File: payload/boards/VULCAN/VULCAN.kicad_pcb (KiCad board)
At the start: 2 copper layers, 63.5 x 101.6 mm, 74 parts, among them IC1 LT1001CS8#PBF, J1 POWER, J2 I2C, J3 Serial, J4 SPI, J5 GPIO, J6 XT60PW-M, J7 Screw_Terminal_01x06, J8 Screw_Terminal_01x06, J9 FAN, Q1 2N7002K, U1 DS18B20, U2 AZ1117IH-5.0TRG1, U3 AP63357, U4 MPXV7002DP, U5 DEV-16771, U6 MAX31850KATB+T, U7 MAX31850KATB+T, U8 MAX31850KATB+T

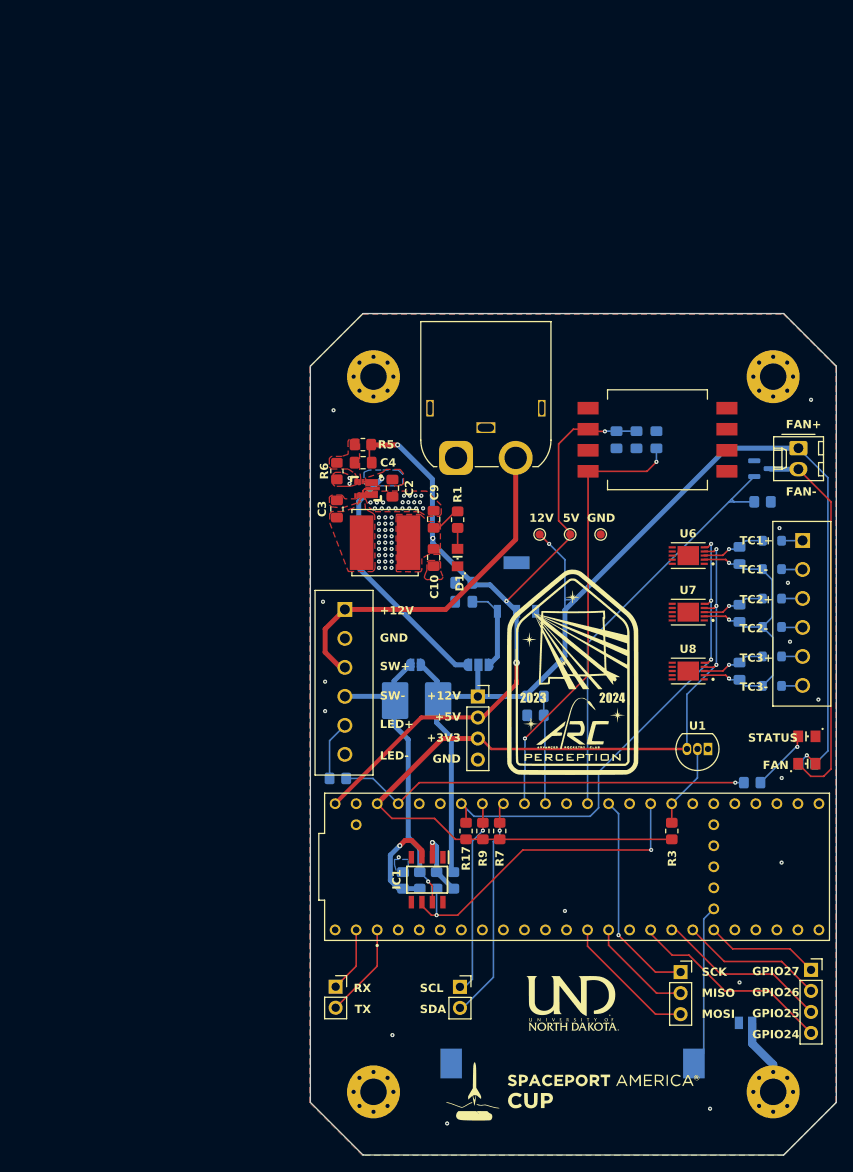
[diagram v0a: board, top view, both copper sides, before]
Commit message: rework
boost converter stuff
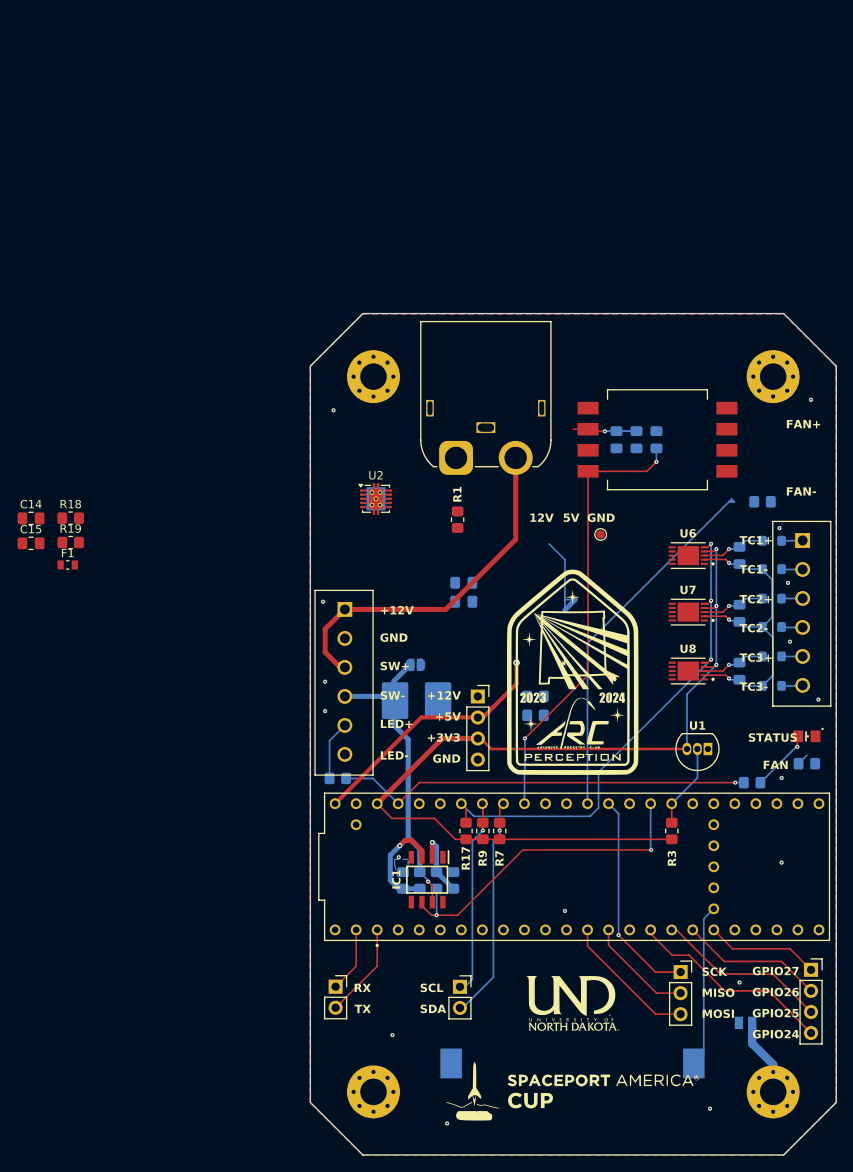
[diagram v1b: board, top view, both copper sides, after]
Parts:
- removed C10, C9: 22uF, Capacitor_SMD:C_0805_2012Metric_Pad1.18x1.45mm_HandSolder
- removed C2: 10uF, Capacitor_SMD:C_0805_2012Metric_Pad1.18x1.45mm_HandSolder
- removed C3: 0.1u, Capacitor_SMD:C_0805_2012Metric_Pad1.18x1.45mm_HandSolder
- removed C4: 47pF, Capacitor_SMD:C_0805_2012Metric_Pad1.18x1.45mm_HandSolder
- removed D1: OSRAM_LSR976-NR-1, Skyhawkson_Footprints:OSRAM_0805
- removed D3: CMD17-21VGD/TR8, Skyhawkson_Footprints:OSRAM_0805
- removed J9: FAN, CustomFootprintLib:Molex_KK-254_AE-6410-02A_1x02_P2.54mm_Vertical
- removed JP1: Jumper_3_Open, Jumper:SolderJumper-3_P1.3mm_Open_RoundedPad1.0x1.5mm
- removed L1: 6.8uH, CustomFootprintLib:IND_SRN8040TA-6R8M
- removed Q1: 2N7002K, Package_TO_SOT_SMD:SOT-23
- removed R5: 220k, Resistor_SMD:R_0805_2012Metric_Pad1.20x1.40mm_HandSolder
- removed R6: 41.2k, Resistor_SMD:R_0805_2012Metric_Pad1.20x1.40mm_HandSolder
- removed TP2: VIN, TestPoint:TestPoint_Pad_D1.0mm
- removed TP3: +5V, TestPoint:TestPoint_Pad_D1.0mm
- removed U3: AP63357, CustomFootprintLib:AP63356 (V-DFN3020-13)
- added C14: 10uF, Capacitor_SMD:C_0805_2012Metric_Pad1.18x1.45mm_HandSolder, F.Cu at (118.7, 70.5)
- added C15: 10uF, Capacitor_SMD:C_0805_2012Metric_Pad1.18x1.45mm_HandSolder, F.Cu at (118.7, 73.5)
- added F1: LF_0494003, Skyhawkson_Footprints:LF_0494_(0603), F.Cu at (123.1, 76.1)
- added R18: 2M, Resistor_SMD:R_0805_2012Metric_Pad1.20x1.40mm_HandSolder, F.Cu at (123.5, 70.4)
- added R19: 220k, Resistor_SMD:R_0805_2012Metric_Pad1.20x1.40mm_HandSolder, F.Cu at (123.5, 73.4)
- C1: value 22uF -> 10uF
- C5: value 10uF -> 1uF
- R10: value 500 -> 2M
- R8: value 470 -> 220k
- U2: value AZ1117IH-5.0TRG1 -> TPS61200DRC; footprint CustomFootprintLib:SOT223-5_DIO -> Package_SON:Texas_S-PVSON-N10_ThermalVias; moved to F.Cu
- moved U2 20.0 mm to (160.3, 68.1), turned to 0 degrees
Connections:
- net /+12V_RAW renamed /VBAT_SWITCH
- net /+BATT_RAW renamed /VBAT
- net /DS18_TEMP renamed /BOARD_TEMP
- C1 pad 1: +5V -> GND
- C1 pad 2: GND -> /VCC
- C12 pad 1: +5V -> /+5V
- C13 pad 1: +5V -> /+5V
- C5 pad 1: 5V_LDO -> Net-(U2-VAUX)
- J1 pad 2: +5V -> /+5V
- JP3 pad 1: /+12V -> /VCC
- R1 pad 1: +5V -> /+5V
- R10 pad 1: /+12V -> /+5V
- R10 pad 2: Net-(D3-PadA) -> Net-(U2-FB)
- R11 pad 1: /+12V -> /VCC
- R11 pad 2: /VBAT_SENSE -> /VCC_SENSE
- R12 pad 1: /VBAT_SENSE -> /VCC_SENSE
- R14 pad 1: /+12V -> /VCC
- R8 pad 1: GND -> Net-(U2-FB)
- R8 pad 2: /FAN -> GND
- R_Shunt1 pad 1: /+12V -> /VCC
- U2 pad 1: GND -> Net-(U2-VAUX)
- U2 pad 2: +5V -> /+5V
- U2 pad 3: 5V_LDO -> Net-(U2-L)
- U2 pad 4: unconnected-(U2-VOUT-Pad4) -> GND
- U4 pad 2: +5V -> /+5V
- U5 pad VIN: +5V -> /+5V
- U6 pad 6: unconnected-(U6-AD0-Pad6) -> GND
- U6 pad 7: unconnected-(U6-AD1-Pad7) -> GND
- U6 pad 8: unconnected-(U6-AD2-Pad8) -> GND
- U6 pad 9: unconnected-(U6-AD3-Pad9) -> GND
- U7 pad 6: unconnected-(U7-AD0-Pad6) -> +3V3
- U7 pad 7: unconnected-(U7-AD1-Pad7) -> GND
- U7 pad 8: unconnected-(U7-AD2-Pad8) -> GND
- U7 pad 9: unconnected-(U7-AD3-Pad9) -> GND
- U8 pad 6: unconnected-(U8-AD0-Pad6) -> GND
- U8 pad 7: unconnected-(U8-AD1-Pad7) -> +3V3
- U8 pad 8: unconnected-(U8-AD2-Pad8) -> GND
- U8 pad 9: unconnected-(U8-AD3-Pad9) -> GND
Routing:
- net /+12V: track 142.5 -> 11.8 mm, vias 1 -> 0
- net +5V: track 105.8 -> 0.00 mm, vias 5 -> 0
- net Net-(J9-Pin_2): track 46.2 -> 0.00 mm
- net /+5V: track 0.00 -> 37.8 mm, vias 0 -> 2
- net 5V_BUCK: track 30.9 -> 0.00 mm, vias 1 -> 0
- net /VBAT_SENSE: track 13.0 -> 0.00 mm
- net 5V_LDO: track 10.4 -> 0.00 mm
- net /FAN: track 51.3 -> 45.1 mm
- net Net-(D3-PadA): track 2.90 -> 0.00 mm, vias 1 -> 0
- net Net-(D1-PadA): track 2.51 -> 0.00 mm
- net Net-(U3-SW): track 1.87 -> 0.00 mm
- net Net-(U2-FB): track 0.00 -> 1.41 mm
- net /I2C_SCL: track 24.1 -> 23.0 mm
- net /I2C_SDA: track 27.5 -> 26.7 mm
- net GND: track 0.28 -> 0.00 mm, vias 65 -> 17
- removed copper zone on F.Cu, net +5V
- removed copper zone on B.Cu, net 5V_BUCK
- removed copper zone on F.Cu, net 5V_BUCK
- removed copper zone on F.Cu, net Net-(U3-BST)
- removed copper zone on F.Cu, net Net-(U3-FB)
- removed copper zone on F.Cu, net Net-(U3-SW)

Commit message: reverted back to bucks
since we need weight in the form of batteries
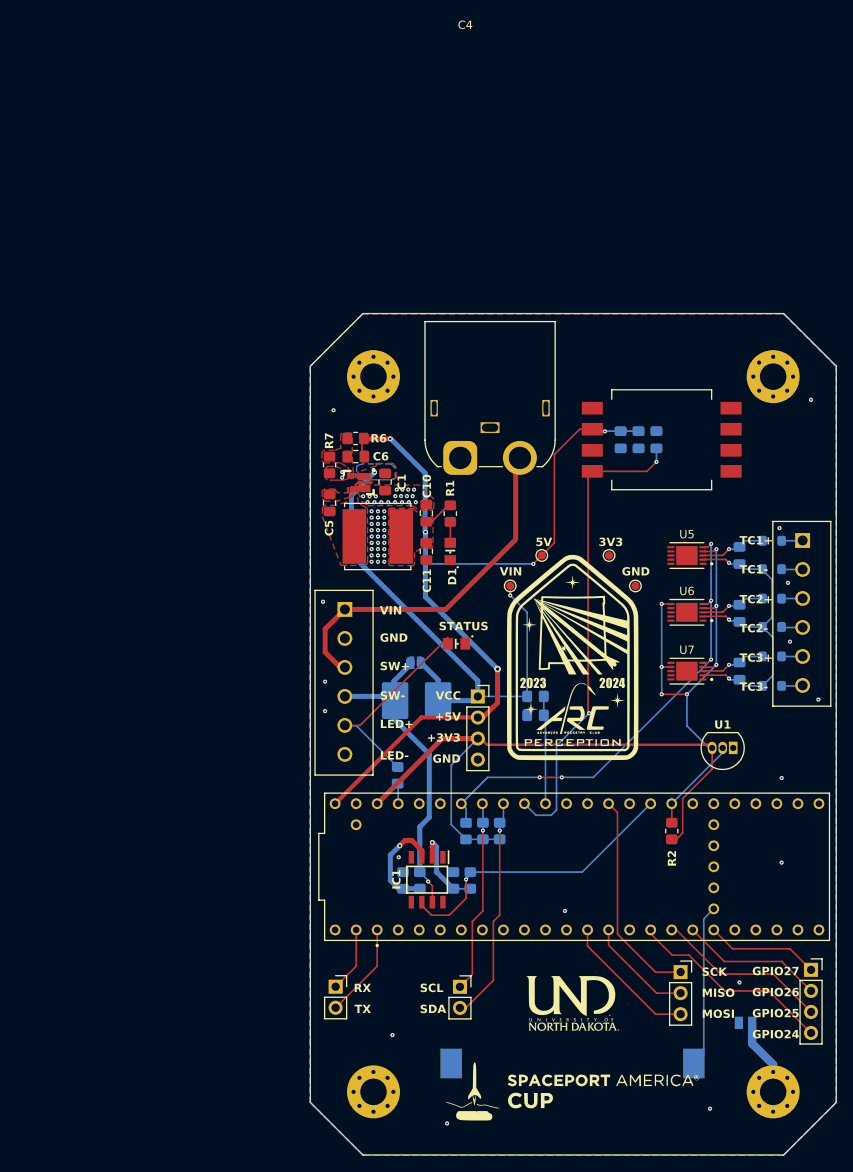
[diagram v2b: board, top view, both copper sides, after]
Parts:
- removed C12: 0.01uF, Capacitor_SMD:C_0805_2012Metric_Pad1.18x1.45mm_HandSolder
- removed C13: 1.0uF, Capacitor_SMD:C_0805_2012Metric_Pad1.18x1.45mm_HandSolder
- removed C14, C15: 10uF, Capacitor_SMD:C_0805_2012Metric_Pad1.18x1.45mm_HandSolder
- removed F1: LF_0494003, Skyhawkson_Footprints:LF_0494_(0603)
- removed JP3: Jumper_2_Open, Jumper:SolderJumper-2_P1.3mm_Open_RoundedPad1.0x1.5mm
- removed the R10 at (212.3, 100.1)
- removed R15, R16: 5K, Resistor_SMD:R_0805_2012Metric_Pad1.20x1.40mm_HandSolder
- removed R17: 4.7k, Resistor_SMD:R_0805_2012Metric_Pad1.20x1.40mm_HandSolder
- removed R18: 2M, Resistor_SMD:R_0805_2012Metric_Pad1.20x1.40mm_HandSolder
- removed R19: 220k, Resistor_SMD:R_0805_2012Metric_Pad1.20x1.40mm_HandSolder
- removed the R2 at (205.7, 102.4)
- removed the R4 at (155.7, 101.9)
- removed the U2 at (160.3, 68.1)
- removed U8: MAX31850KATB+T, CustomFootprintLib:SON50P300X400X80-11N
- added C10: 22uF, Capacitor_SMD:C_0805_2012Metric_Pad1.18x1.45mm_HandSolder, F.Cu at (166.4, 69.8)
- added C11: 22uF, Capacitor_SMD:C_0805_2012Metric_Pad1.18x1.45mm_HandSolder, F.Cu at (166.4, 74.4)
- added C3: 0.01uF, Capacitor_SMD:C_0805_2012Metric_Pad1.18x1.45mm_HandSolder, B.Cu at (192.0, 61.0)
- added C4: 1.0uF, Capacitor_SMD:C_0805_2012Metric_Pad1.18x1.45mm_HandSolder, B.Cu at (189.9, 61.0)
- added C6: 47pF, Capacitor_SMD:C_0805_2012Metric_Pad1.18x1.45mm_HandSolder, F.Cu at (157.9, 63.0)
- added D1: CMD17-21VRD/TR8, Skyhawkson_Footprints:OSRAM_0805, F.Cu at (169.3, 74.4)
- added JP1: Jumper_2_Open, Jumper:SolderJumper-2_P1.3mm_Open_RoundedPad1.0x1.5mm, B.Cu at (165.1, 87.9)
- added L1: 6.8uH, CustomFootprintLib:IND_SRN8040TA-6R8M, F.Cu at (160.5, 72.6)
- added R11: R, Resistor_SMD:R_0805_2012Metric_Pad1.20x1.40mm_HandSolder, B.Cu at (162.9, 101.5)
- added R14: 4.7k, Resistor_SMD:R_0805_2012Metric_Pad1.20x1.40mm_HandSolder, B.Cu at (171.2, 108.2)
- added R5: 5K, Resistor_SMD:R_0805_2012Metric_Pad1.20x1.40mm_HandSolder, B.Cu at (163.6, 114.2)
- added R6: 220k, Resistor_SMD:R_0805_2012Metric_Pad1.20x1.40mm_HandSolder, F.Cu at (157.9, 60.8)
- added R7: 41.2k, Resistor_SMD:R_0805_2012Metric_Pad1.20x1.40mm_HandSolder, F.Cu at (154.7, 64.0)
- added TP2: +5V, TestPoint:TestPoint_Pad_D1.0mm, F.Cu at (180.3, 74.9)
- added TP3: +3.3V, TestPoint:TestPoint_Pad_D1.0mm, F.Cu at (188.5, 74.9)
- added TP4: VIN, TestPoint:TestPoint_Pad_D1.0mm, F.Cu at (176.5, 78.6)
- added U3: AP63357, CustomFootprintLib:AP63356 (V-DFN3020-13), F.Cu at (158.2, 66.1)
- added U5: MAX31850KATB+T, CustomFootprintLib:SON50P300X400X80-11N, F.Cu at (197.9, 74.9)
- C1: moved to F.Cu
- C5: value 1uF -> 0.1u; moved to F.Cu
- R12: renamed from R7; moved to B.Cu
- R13: renamed from R9; moved to B.Cu
- R8: value 220k -> 5K
- U2: renamed from U4; value MPXV7002DP -> MAX31850KATB+T
- moved R8 57.8 mm to (171.7, 114.2), turned to -90 degrees
- moved D2 43.7 mm to (170.1, 85.6)
- moved C5 20.1 mm to (154.7, 68.6), turned to -90 degrees
- moved C1 15.4 mm to (161.4, 66.1), turned to -90 degrees
- moved TP1 7.50 mm to (191.6, 78.6), turned to -90 degrees
- moved U7 7.13 mm to (197.9, 88.9)
- moved U6 6.85 mm to (197.9, 81.8)
- moved U1 3.05 mm to (203.5, 98.2)
- moved G1 1.78 mm to (184.2, 87.1)
- moved R1 1.15 mm to (169.3, 69.9)
- moved U2 0.51 mm to (194.8, 61.0)
- moved J6 0.51 mm to (170.5, 63.1)
- renumbered C11 to C2, C6 to C7, C7 to C8, C8 to C9, R12 to R10, R3 to R2, R13 to R3, R14 to R4, R11 to R9, U5 to U4
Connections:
- net /VBAT_SWITCH renamed /VBAT_SW
- C1 pad 1: GND -> /VCC
- C1 pad 2: /VCC -> GND
- C5 pad 2: GND -> Net-(U3-SW)
- D2 pad A: Net-(D2-PadA) -> /LED_G_RES
- J1 pad 1: /+12V -> /VCC
- J7 pad 5: Net-(J7-Pin_5) -> /LED_G_RES
- R8 pad 1: Net-(U2-FB) -> /VBAT_CURRENT_SENSE
- R8 pad 2: GND -> Net-(IC1--IN)
- U4 pad 16: /VBAT_SENSE -> /VCC_SENSE
- U6 pad 3: /T1 -> /T2
- U6 pad 6: GND -> +3V3
- U7 pad 3: /T2 -> /T3
- U7 pad 6: +3V3 -> GND
- U7 pad 7: GND -> +3V3
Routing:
- net /+5V: track 37.8 -> 109.8 mm, vias 2 -> 5
- net /VCC: track 0.00 -> 66.1 mm, vias 0 -> 2
- net /LED_GREEN: track 50.3 -> 2.46 mm, vias 1 -> 0
- net /FAN: track 45.1 -> 0.00 mm
- net /LED_G_RES: track 0.00 -> 25.3 mm
- net +3V3: track 108.5 -> 124.0 mm, vias 3 -> 7
- net /VCC_SENSE: track 0.00 -> 13.0 mm
- net /+12V: track 11.8 -> 0.00 mm
- net Net-(J7-Pin_5): track 7.17 -> 0.00 mm
- net Net-(D2-PadA): track 7.14 -> 0.00 mm, vias 1 -> 0
- net /VBAT_CURRENT_SENSE: track 40.2 -> 35.2 mm, vias 2 -> 1
- net /PITOT: track 53.7 -> 57.6 mm
- net /TC_DATA: track 60.7 -> 56.9 mm, vias 3 -> 5
- net Net-(D1-PadA): track 0.00 -> 2.51 mm
- net Net-(IC1--IN): track 8.39 -> 10.4 mm
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- added copper zone on B.Cu, net (none)
- added copper zone on F.Cu, net /+5V
- added copper zone on F.Cu, net /VCC
- added copper zone on F.Cu, net Net-(U3-BST)
- added copper zone on F.Cu, net Net-(U3-FB)
- added copper zone on F.Cu, net Net-(U3-SW)
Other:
- board text added: "3V3"
- board text added: "VCC"
- board text added: "VIN"
- board text removed: "+12V"
- board text removed: "12V"
- board text removed: "12V FAN ONLY"
- board text removed: "BUCK"
- board text removed: "FAN"
- board text removed: "FAN+"
- board text removed: "FAN-"
- board text removed: "LDO"
- board text removed: "PSU 12.6V"

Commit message: updates
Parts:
- removed the J6 at (170.5, 63.1)
- added C1: 22uF, Capacitor_SMD:C_0805_2012Metric_Pad1.18x1.45mm_HandSolder, B.Cu at (185.9, 92.6)
- added C14: 0.1uF, Capacitor_SMD:C_0805_2012Metric_Pad1.18x1.45mm_HandSolder, B.Cu at (197.9, 72.0)
- added C15: 0.1uF, Capacitor_SMD:C_0805_2012Metric_Pad1.18x1.45mm_HandSolder, B.Cu at (197.9, 86.0)
- added C16: 0.1uF, Capacitor_SMD:C_0805_2012Metric_Pad1.18x1.45mm_HandSolder, B.Cu at (197.9, 78.9)
- added C2: 10uF, Capacitor_SMD:C_0805_2012Metric_Pad1.18x1.45mm_HandSolder, B.Cu at (185.9, 94.7)
- added D3: SPHV12-01ETG-C, PCM_Diode_SMD_Handsoldering_AKL:D_SOD-882_DFN1006-2_TVS, B.Cu at (156.5, 78.5)
- added D4: BAT165A, Diode_SMD:D_SOD-323_HandSoldering, B.Cu at (153.9, 87.1)
- added F1: 1.5A, Fuse:Fuse_0805_2012Metric_Pad1.15x1.40mm_HandSolder, B.Cu at (153.9, 82.5)
- added J1: XT60PW-M, CustomFootprintLib:AMASS_XT60PW-M, F.Cu at (174.1, 56.6)
- added JP1: Jumper_2_Open, Jumper:SolderJumper-2_P1.3mm_Open_RoundedPad1.0x1.5mm, B.Cu at (172.6, 86.0)
- added JP3: Jumper_2_Open, CustomFootprintLib:SolderJumper, B.Cu at (166.8, 51.4)
- added JP4: Jumper_2_Open, CustomFootprintLib:SolderJumper, B.Cu at (201.5, 50.8)
- added JP5: Jumper_2_Open, CustomFootprintLib:SolderJumper, B.Cu at (166.3, 142.8)
- added U1: AZ1117IH-5.0TRG1, CustomFootprintLib:SOT223-5_DIO, B.Cu at (178.8, 92.5)
- C10: renamed from C8; value 0.1uF -> 0.01uF
- C11: renamed from C9; value 0.1uF -> 0.01uF
- C12: renamed from C10; moved to B.Cu
- C13: renamed from C11; moved to B.Cu
- C7: renamed from C5; value 0.1u -> 0.1uF
- C9: renamed from C7; value 0.1uF -> 0.01uF
- FB1, FB2, FB3, FB4, FB5, FB6: value Ferrite_Bead -> 2508056017Y2
- R1: moved to B.Cu
- moved R6 16.9 mm to (162.4, 77.0), turned to 0 degrees
- moved R7 14.6 mm to (165.6, 73.7), turned to 90 degrees
- moved C13 13.2 mm to (157.3, 64.8), turned to 0 degrees
- moved C8 12.7 mm to (162.4, 74.9), turned to 0 degrees
- moved JP6 11.8 mm to (202.0, 142.7)
- moved D1 11.0 mm to (172.8, 84.9), turned to 0 degrees
- moved C7 10.9 mm to (165.6, 68.9), turned to 90 degrees
- moved R1 9.97 mm to (162.4, 77.1), turned to 0 degrees
- moved C12 9.46 mm to (157.3, 67.1), turned to 0 degrees
- moved L1 7.48 mm to (159.8, 65.2), turned to 180 degrees
- moved U4 6.78 mm to (162.1, 71.7), turned to 0 degrees
- moved C3 6.25 mm to (158.9, 71.8), turned to 90 degrees
- moved R9 5.89 mm to (178.8, 97.8)
- moved R10 5.64 mm to (178.8, 99.8)
- moved D2 3.16 mm to (172.8, 87.2)
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- renumbered C1 to C3, C2 to C4, C3 to C5, C4 to C6, C6 to C8, J1 to J2, J2 to J3, J3 to J4, J4 to J5, J5 to J6, JP1 to JP2, JP2 to JP6, U1 to U2, U2 to U3, U3 to U4, U4 to U5, U5 to U6, U6 to U7, U7 to U8
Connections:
- net /LED_GREEN renamed /LED_GRN
- net /LED_G_RES renamed /LED_GRN_RES
- C3 pad 1: /VCC -> Net-(JP1-B)
- H1 pad 1: unconnected-(H1-Pad1) -> Net-(JP3-A)
- H2 pad 1: unconnected-(H2-Pad1)_7 -> Net-(JP4-A)
- H3 pad 1: unconnected-(H3-Pad1)_0 -> Net-(JP5-A)
- J7 pad 3: /VBAT -> /VBAT_RP
- U4 pad 1: /VCC -> Net-(JP1-B)
- U4 pad 2: /VCC -> Net-(JP1-B)
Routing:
- net /+5V: track 109.8 -> 126.7 mm, vias 5 -> 13
- net Net-(JP1-B): track 0.00 -> 16.5 mm, vias 0 -> 3
- net Net-(D1-PadA): track 2.51 -> 13.1 mm, vias 0 -> 1
- net +3V3: track 124.0 -> 132.2 mm, vias 7 -> 11
- net Net-(JP4-A): track 0.00 -> 7.07 mm
- net Net-(JP3-A): track 0.00 -> 6.86 mm
- net Net-(JP5-A): track 0.00 -> 6.77 mm
- net /VCC: track 66.1 -> 72.4 mm, vias 2 -> 1
- net /VCC_SENSE: track 13.0 -> 7.33 mm
- net Net-(U4-FB): track 0.00 -> 3.17 mm
- net /VBAT: track 42.7 -> 39.7 mm
- net Net-(JP6-A): track 6.98 -> 4.37 mm
- net /VBAT_RP: track 0.00 -> 2.56 mm
- net Net-(D4-A): track 0.00 -> 2.30 mm
- net GND: track 0.28 -> 2.42 mm, vias 65 -> 145
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- added copper zone on B.Cu, net /+5V
- added copper zone on B.Cu, net Net-(JP1-B)
- added copper zone on F.Cu, net Net-(JP1-B)
- removed copper zone on B.Cu, net (none)
- removed copper zone on F.Cu, net /VCC
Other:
- board text added: "BUCK"
- board text added: "PWR"
- board text added: "PWR 12.6V"
- board text added: "STAT"
- board text removed: "${REFERENCE}"
- board text removed: "Mounting Hole"
- board text removed: "STATUS"
